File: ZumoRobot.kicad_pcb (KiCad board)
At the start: 2 copper layers, 50 x 50 mm, 54 parts, among them CN1 B2B-XH-A, CN2 B2B-XH-A, CN3 B2B-XH-A, CN4 B2B-XH-A, SW1 TS-1088-AR02016, SW2 TS-1088-AR02016, U1 ESP32-S3-WROOM-1, U2 TPS62172DSG, U4 DRV8870DDA, U5 DRV8870DDA

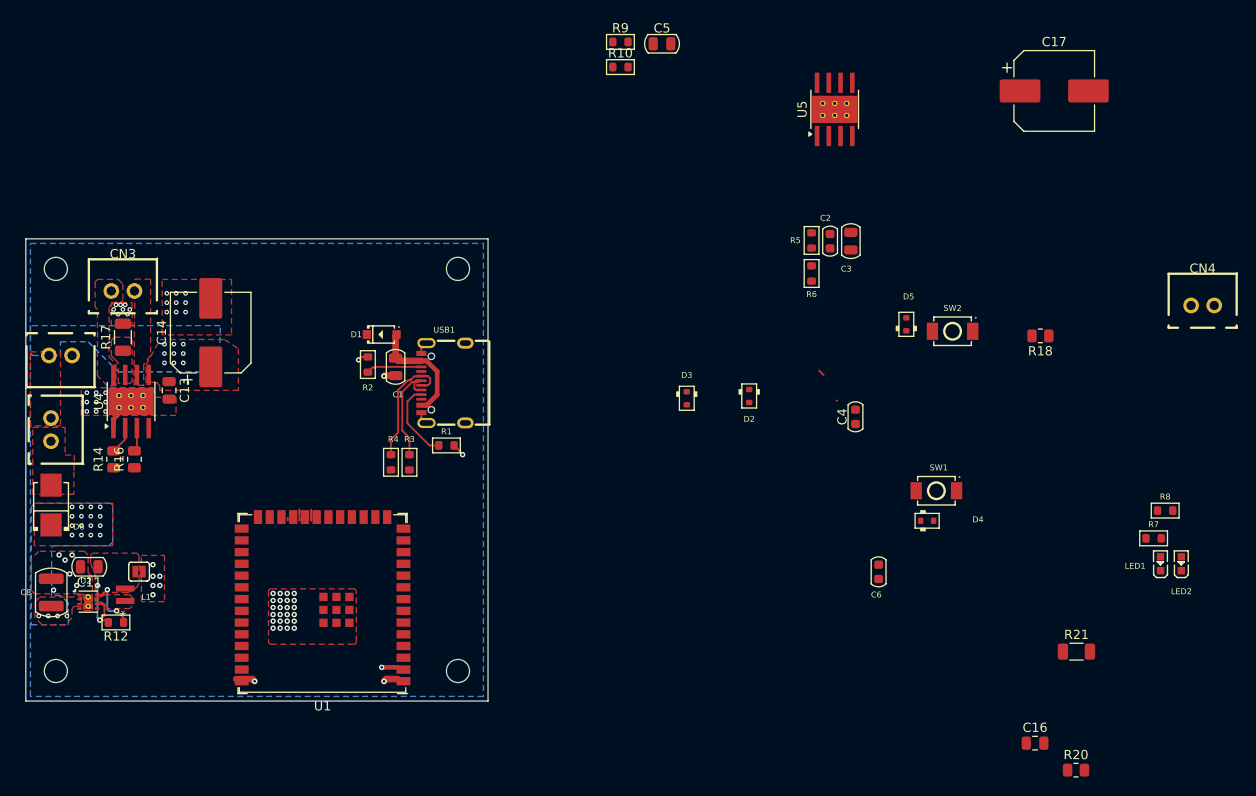
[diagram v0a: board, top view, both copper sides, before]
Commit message: change motor driver
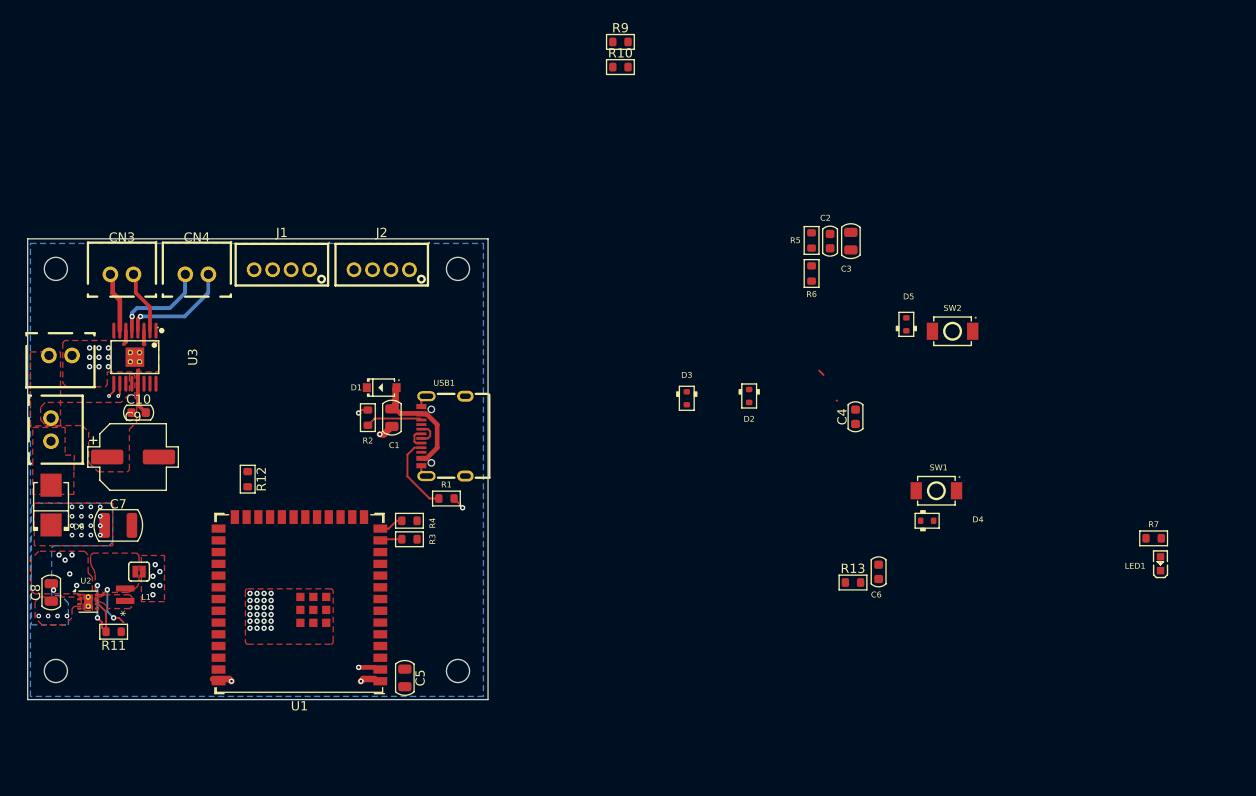
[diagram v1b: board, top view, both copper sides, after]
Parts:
- removed C11: 22uF 25V, PCM_Capacitor_SMD_AKL:C_0805_2012Metric
- removed C13, C16: C, Capacitor_SMD:C_0805_2012Metric
- removed C14, C17: C_Polarized, Capacitor_SMD:CP_Elec_8x10.5
- removed LED2: XL-1608SURC-06, EasyEDA:LED0603-RD_RED
- removed R14, R16, R18, R20: R_US, Resistor_SMD:R_0805_2012Metric
- removed R17, R21: R_US, Resistor_SMD:R_1206_3216Metric
- removed R8: 10K, PCM_Resistor_SMD_AKL:R_0603_1608Metric
- removed U4, U5: DRV8870DDA, Package_SO:Texas_HTSOP-8-1EP_3.9x4.9mm_P1.27mm_EP2.95x4.9mm_Mask2.4x3.1mm_ThermalVias
- added C10: C_0603, PCM_Capacitor_SMD_AKL:C_0603_1608Metric, F.Cu at (188.5, 98.9)
- added C7: 10uF 25V, PCM_Capacitor_SMD_AKL:C_1210_3225Metric, F.Cu at (186.3, 111.1)
- added C9: CP_SMD_D6.3mm_H5.4mm, PCM_Capacitor_SMD_AKL:CP_Elec_6.3x5.4, F.Cu at (187.9, 103.7)
- added J1: Conn_01x04_Socket, EasyEDA:CONN-TH_B4B-PH-K-S, F.Cu at (204.0, 83.4)
- added J2: Conn_01x04_Socket, EasyEDA:CONN-TH_B4B-PH-K-S, F.Cu at (214.8, 83.4)
- added R11: 100k, PCM_Resistor_SMD_AKL:R_0603_1608Metric, F.Cu at (185.8, 122.6)
- added R13: 10K, PCM_Resistor_SMD_AKL:R_0603_1608Metric, F.Cu at (265.8, 117.3)
- added U3: DRV8411APWPR, EasyEDA:HTSSOP-16_L5.0-W4.4-P0.65-LS6.4-TL-EP-1, F.Cu at (188.1, 92.9)
- C8: value 10uF 25V -> 22uF 25V; footprint PCM_Capacitor_SMD_AKL:C_1210_3225Metric -> PCM_Capacitor_SMD_AKL:C_0805_2012Metric
- R12: value 100k -> 10K
- moved CN4 108.9 mm to (194.8, 83.9)
- moved C5 74.0 mm to (217.3, 127.6), turned to -90 degrees
- moved R12 21.1 mm to (200.3, 106.1), turned to -90 degrees
- moved R3 8.32 mm to (217.8, 112.6), turned to 180 degrees
- moved R4 6.63 mm to (217.8, 110.6), turned to 180 degrees
- moved D1 5.74 mm to (214.8, 96.2)
- moved R1 5.74 mm to (221.8, 108.2)
- moved R2 5.74 mm to (213.3, 99.4)
- moved USB1 5.74 mm to (221.5, 101.4)
- moved C1 5.51 mm to (215.9, 99.4)
- moved U1 2.50 mm to (205.9, 119.7)
- moved CN3 1.80 mm to (186.7, 83.9)
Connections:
- C8 pad 1: VCC -> /PowerRails/Reg3v3_out
- CN3 pad 1: /PH3A_Driver/M1 -> /DRV8411APWR/M1A
- CN3 pad 2: /PH3A_Driver/M2 -> /DRV8411APWR/M1B
- CN4 pad 1: /PH3A_Driver1/M1 -> /DRV8411APWR/M2A
- CN4 pad 2: /PH3A_Driver1/M2 -> /DRV8411APWR/M2B
- D1 pad 2: +5V -> VCC
- R12 pad 1: /PowerRails/PG2 -> +3V3
- R12 pad 2: /PowerRails/Reg3v3_out -> /Motor_Fault
- U1 pad 15: unconnected-(U1-GPIO3/TOUCH3/ADC1_CH2-Pad15) -> /PWMA1
- U1 pad 16: unconnected-(U1-GPIO46-Pad16) -> /PWMA2
- U1 pad 17: unconnected-(U1-GPIO9/TOUCH9/ADC1_CH8/FSPIHD/SUBSPIHD-Pad17) -> /PWMB2
- U1 pad 18: unconnected-(U1-GPIO10/TOUCH10/ADC1_CH9/FSPICS0/FSPIIO4/SUBSPICS0-Pad18) -> /PWMB1
- U1 pad 19: unconnected-(U1-GPIO11/TOUCH11/ADC2_CH0/FSPID/FSPIIO5/SUBSPID-Pad19) -> /IN-ToF1
- U1 pad 20: unconnected-(U1-GPIO12/TOUCH12/ADC2_CH1/FSPICLK/FSPIIO6/SUBSPICLK-Pad20) -> /IN-ToF2
- U1 pad 21: unconnected-(U1-GPIO13/TOUCH13/ADC2_CH2/FSPIQ/FSPIIO7/SUBSPIQ-Pad21) -> /IN-ToF3
- U1 pad 22: unconnected-(U1-GPIO14/TOUCH14/ADC2_CH3/FSPIWP/FSPIDQS/SUBSPIWP-Pad22) -> /IN-ToF4
- U1 pad 38: /SERVO_PWM -> unconnected-(U1-GPIO2/TOUCH2/ADC1_CH1-Pad38)
- U1 pad 6: unconnected-(U1-GPIO6/TOUCH6/ADC1_CH5-Pad6) -> /Motor_Fault
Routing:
- net /DRV8411APWR/M2A: track 0.00 -> 12.0 mm, vias 0 -> 1
- net /DRV8411APWR/M2B: track 0.00 -> 10.6 mm, vias 0 -> 1
- net /DP: track 13.1 -> 2.67 mm
- net /DN: track 12.0 -> 2.33 mm
- net /DRV8411APWR/M1A: track 0.00 -> 6.82 mm
- net /DRV8411APWR/M1B: track 0.00 -> 6.51 mm
- net GND: track 13.9 -> 18.7 mm, vias 61 -> 44
- net /PH3A_Driver/in2_ic: track 2.98 -> 0.00 mm
- net /USB_D+: track 0.00 -> 2.68 mm
- net /PH3A_Driver/in1_ic: track 2.57 -> 0.00 mm
- net /USB_D-: track 0.00 -> 2.37 mm
- net unconnected-(U1-GPIO13/TOUCH13/ADC2_CH2/FSPIQ/FSPIIO7/SUBSPIQ-Pad21): track 2.28 -> 0.00 mm
- net unconnected-(U1-GPIO14/TOUCH14/ADC2_CH3/FSPIWP/FSPIDQS/SUBSPIWP-Pad22): track 1.66 -> 0.00 mm
- net /PWMB1: track 0.00 -> 1.55 mm, vias 0 -> 1
- net /PWMB2: track 0.00 -> 1.40 mm, vias 0 -> 1
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- removed copper zone on B.Cu, net +BATT
- removed copper zone on F.Cu, net /PH3A_Driver/ISENSE
- removed copper zone on F.Cu, net /PH3A_Driver/M1
- removed copper zone on F.Cu, net /PH3A_Driver/M2
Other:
- board size 50 x 50 mm -> 49.8 x 49.8 mm

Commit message: avances
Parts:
- removed J1, J2: Conn_01x04_Socket, EasyEDA:CONN-TH_B4B-PH-K-S
- removed L1: MDMK2020T2R2MM, Snapeda:IND_MDMK2020T1R0MM_TAY
- added L2: LQM2HPN2R2MJ0L, EasyEDA:L1008, F.Cu at (187.0, 118.1)
- added U4: DB125-3.5-4P-GN, EasyEDA:CONN-TH_DB125-3.5-4P-GN, F.Cu at (190.0, 64.4)
- added U5: DB125-3.5-4P-GN, EasyEDA:CONN-TH_DB125-3.5-4P-GN, F.Cu at (204.7, 64.4)
- moved H1 20.2 mm to (179.6, 63.2)
- moved H4 20.2 mm to (223.1, 63.2)
- moved JP1 0.95 mm to (189.5, 116.1)
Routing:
- net +3V3: vias 7 -> 1
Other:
- board size 49.8 x 49.8 mm -> 49.8 x 70 mm

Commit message: avanzes
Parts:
- moved R7 106.8 mm to (191.5, 113.3), turned to 90 degrees
- moved LED1 101.6 mm to (197.9, 105.9), turned to 180 degrees
- moved C3 91.0 mm to (187.2, 126.6)
- moved C2 86.9 mm to (189.7, 126.6)
- moved R6 81.5 mm to (191.8, 126.5), turned to 90 degrees
- moved R5 81.3 mm to (194.3, 126.3)
- moved R13 77.6 mm to (193.2, 90.0), turned to 180 degrees
- moved R9 66.7 mm to (195.9, 108.3)
- moved R10 66.2 mm to (219.3, 124.2), turned to 90 degrees
- moved SW2 62.5 mm to (222.2, 121.0)
- moved D5 61.5 mm to (217.6, 119.0), turned to 180 degrees
- moved SW1 53.5 mm to (222.2, 117.2)
- moved C6 51.2 mm to (217.5, 121.1), turned to 180 degrees
- moved D4 49.7 mm to (224.1, 111.3), turned to 90 degrees
- moved C4 47.2 mm to (220.5, 111.6)
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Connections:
- net /PWMA1 renamed /PWMA+
- net /PWMA2 renamed /PWMA-
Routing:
- net +3V3: track 1.74 -> 76.8 mm, vias 1 -> 6
- net /Motor_Fault: track 0.00 -> 68.1 mm, vias 0 -> 4
- net /BOOT: track 0.68 -> 38.1 mm, vias 0 -> 2
- net VCC: track 0.00 -> 34.2 mm, vias 20 -> 21
- net /PWMA-: track 0.00 -> 30.2 mm, vias 0 -> 2
- net /PWMA+: track 0.00 -> 30.2 mm, vias 0 -> 2
- net +7.5V: track 0.00 -> 29.4 mm
- net /PWMB2: track 1.40 -> 30.7 mm, vias 1 -> 2
- net /PWMB1: track 1.55 -> 30.2 mm, vias 1 -> 2
- net GND: track 18.7 -> 31.5 mm, vias 44 -> 82
- net /PowerRails/Reg3v3_out: track 8.86 -> 21.5 mm
- net /RST: track 0.00 -> 11.9 mm
- net /BATTERY2_LEVEL: track 0.00 -> 10.4 mm
- net Net-(LED1-Pad2): track 0.00 -> 9.84 mm, vias 0 -> 2
- net /DP: track 2.67 -> 10.5 mm
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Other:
- board size 49.8 x 70 mm -> 50.5 x 57 mm

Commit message: terminada
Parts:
- added IR-1: TestPoint, PCM_SparkFun-Connector:TestPoint-1.25mm, F.Cu at (218.0, 113.5)
- added IR-2: TestPoint, PCM_SparkFun-Connector:TestPoint-1.25mm, F.Cu at (200.9, 107.4)
- added IR-3: TestPoint, PCM_SparkFun-Connector:TestPoint-1.25mm, F.Cu at (195.2, 117.0)
- added IR-4: TestPoint, PCM_SparkFun-Connector:TestPoint-1.25mm, F.Cu at (198.9, 108.1)
- added R10: 2.2K, PCM_Resistor_SMD_AKL:R_0603_1608Metric, F.Cu at (207.9, 104.3)
- added R11: 2.2K, PCM_Resistor_SMD_AKL:R_0603_1608Metric, F.Cu at (205.5, 104.3)
- added SCL1: TestPoint, PCM_SparkFun-Connector:TestPoint-1.25mm, F.Cu at (206.2, 107.4)
- added SDA1: TestPoint, PCM_SparkFun-Connector:TestPoint-1.25mm, F.Cu at (207.9, 107.3)
- added X-SHUT1: TestPoint, PCM_SparkFun-Connector:TestPoint-1.25mm, F.Cu at (204.4, 107.4)
- added X-SHUT2: TestPoint, PCM_SparkFun-Connector:TestPoint-1.25mm, F.Cu at (218.0, 115.3)
- added X-SHUT3: TestPoint, PCM_SparkFun-Connector:TestPoint-1.25mm, F.Cu at (202.7, 107.4)
- moved D3 5.66 mm to (210.8, 100.0)
- moved R4 5.44 mm to (213.4, 100.1)
- moved R3 3.89 mm to (216.0, 101.6)
- moved C1 2.74 mm to (215.9, 96.7)
- moved D1 2.74 mm to (214.8, 93.5)
- moved R2 2.74 mm to (213.3, 96.7)
- moved USB1 2.74 mm to (221.5, 98.7)
- moved LED1 0.98 mm to (198.8, 105.9)
- renumbered L2 to L1, R11 to R12, R12 to R13, R13 to R14, R9 to R8, R10 to R9, U4 to U2, U5 to U3, U2 to U4, U3 to U5
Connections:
- net /PWMA+ renamed /PWMA1
- net /PWMA- renamed /PWMA2
- U1 pad 10: unconnected-(U1-GPIO17/U1TXD/ADC2_CH6-Pad10) -> /X-SHUT 3
- U1 pad 11: unconnected-(U1-GPIO18/U1RXD/ADC2_CH7/CLK_OUT3-Pad11) -> /IR-1
- U1 pad 19: /IN-ToF1 -> /SDA TOF
- U1 pad 20: /IN-ToF2 -> /SCL TOF
- U1 pad 21: /IN-ToF3 -> /X-SHUT 1 
- U1 pad 22: /IN-ToF4 -> /X-SHUT 2
- U1 pad 23: unconnected-(U1-GPIO21-Pad23) -> /IR-2
- U1 pad 24: unconnected-(U1-GPIO47/SPICLK_P/SUBSPICLK_P_DIFF-Pad24) -> /X-SHUT 4
- U1 pad 26: unconnected-(U1-GPIO45-Pad26) -> /IR-4
- U1 pad 31: unconnected-(U1-GPIO38/FSPIWP/SUBSPIWP-Pad31) -> /IR-3
- U5 pad : (no net) -> GND
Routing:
- net +3V3: track 76.8 -> 89.7 mm
- net /SCL TOF: track 0.00 -> 5.68 mm
- net /USB_D+: track 8.13 -> 13.7 mm
- net /SDA TOF: track 0.00 -> 5.06 mm
- net /PWMB1: track 30.2 -> 34.4 mm
- net /IR-1: track 0.00 -> 4.09 mm
- net /USB_D-: track 9.40 -> 13.3 mm
- net /X-SHUT 3: track 0.00 -> 3.88 mm
- net /PWMB2: track 30.7 -> 34.4 mm
- net /IR-2: track 0.00 -> 3.58 mm
- net /X-SHUT 2: track 0.00 -> 3.30 mm
- net /X-SHUT 1 : track 0.00 -> 3.17 mm
- net +BATT: track 0.00 -> 3.15 mm
- net Net-(USB1-CC1): track 8.56 -> 11.3 mm
- net /PWMA1: track 30.2 -> 32.5 mm
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
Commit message: 2do intento ignorar .history
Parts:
- C10: value C_0603 -> 100 nf
- C9: value CP_SMD_D6.3mm_H5.4mm -> 10uf
- moved SW1 0.61 mm to (222.8, 117.2)
- moved SW2 0.58 mm to (222.8, 121.0)
- moved R8 0.56 mm to (195.9, 107.8)
- moved D2 0.44 mm to (217.8, 111.0)
- moved C4 0.40 mm to (220.8, 111.8)
- moved C5 0.35 mm to (217.3, 127.8)
- moved JP1 0.23 mm to (189.8, 116.1)
- moved D5 0.22 mm to (217.6, 118.8)
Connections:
- U5 pad : GND -> (no net)
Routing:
- net /BOOT: track 38.1 -> 39.8 mm
- net /RST: track 11.9 -> 13.0 mm
- net +3V3: track 89.7 -> 90.7 mm
- net GND: track 30.8 -> 29.9 mm, vias 82 -> 79
- net VCC: vias 21 -> 18
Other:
- board text added: "+"
- board text added: "3V3_OUT"
- board text added: "BATTERY"
- board text added: "GND"
- board text added: "M1"
- board text added: "M2"
